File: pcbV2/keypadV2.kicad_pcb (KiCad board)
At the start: 2 copper layers, 93.7 x 93.3 mm, 78 parts, among them J1 Conn_01x02_Female, J2 USB_C_Receptacle, J3 Conn_01x03_Male, Q1 Q_NMOS_GSD, SW1 SW_Push, SW10 SW_Push, SW11 SW_Push, SW12 SW_Push, SW13 SW_SPDT, SW14 SW_Push, SW15 SW_Push, SW16 SW_Push, SW17 SW_DIP_x03, SW2 SW_Push, SW3 SW_Push, SW4 SW_Push, SW5 SW_Push, SW6 SW_Push, SW7 SW_Push, SW8 SW_Push, SW9 SW_Push, U1 Teensy4.0, U2 Waveshare_OLED_RGB

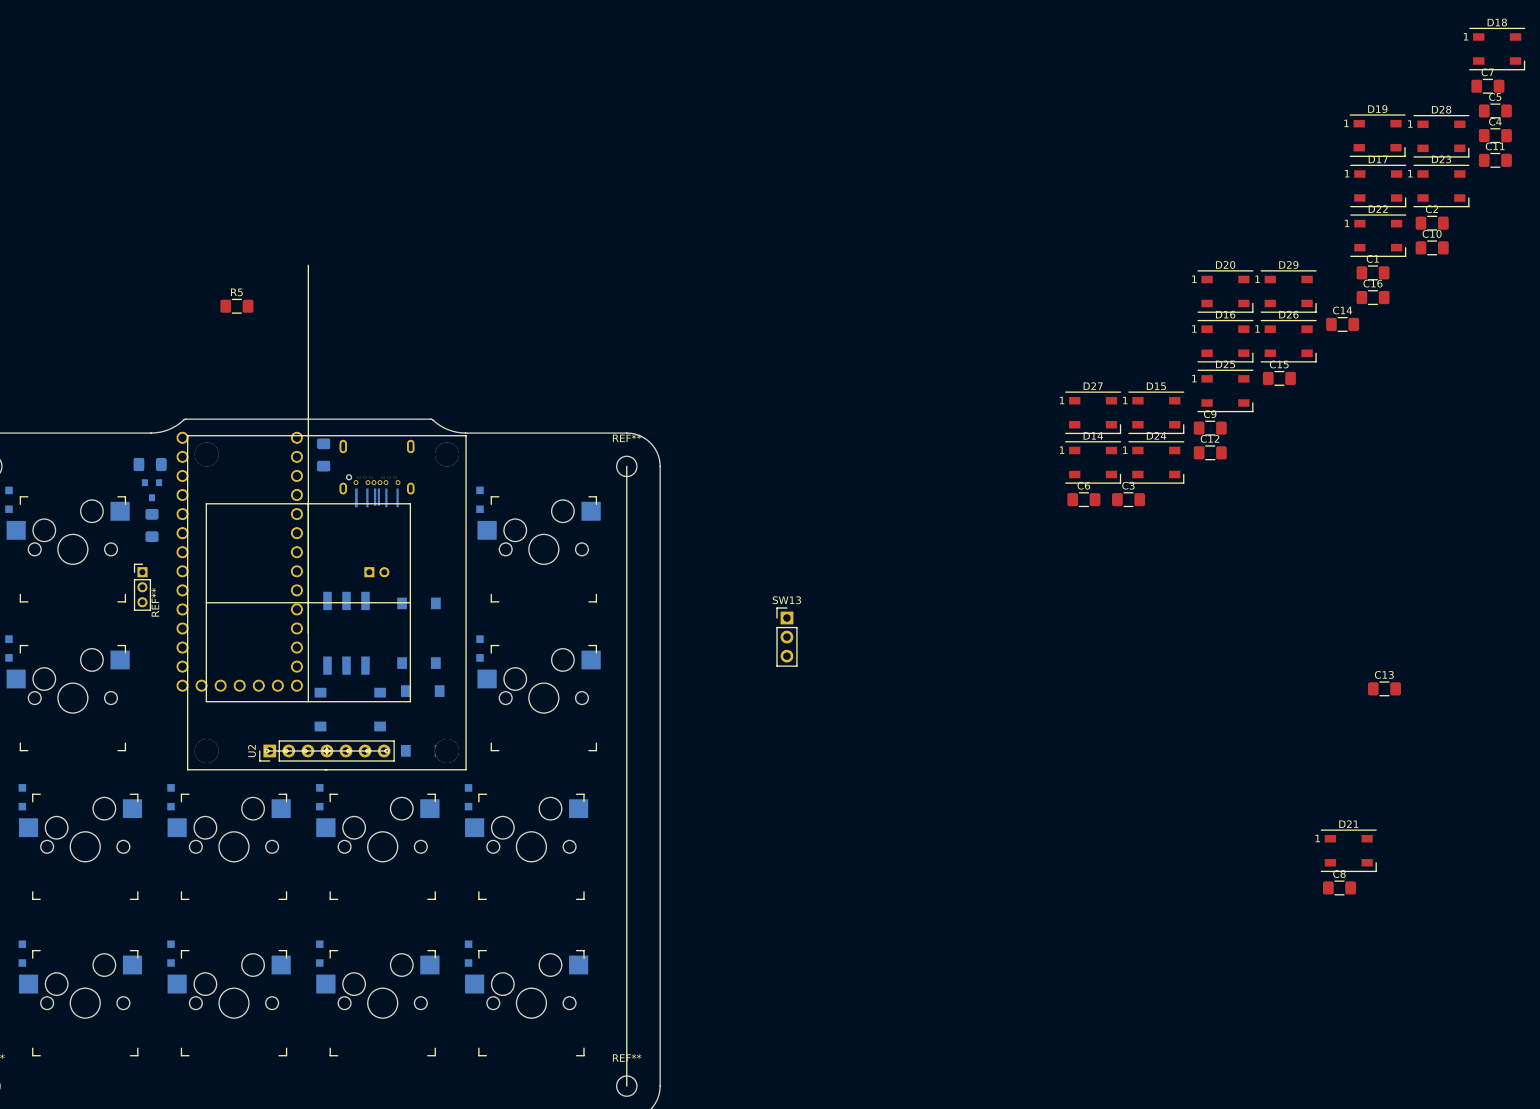
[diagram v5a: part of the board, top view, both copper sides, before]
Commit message: added ws2812b cutouts
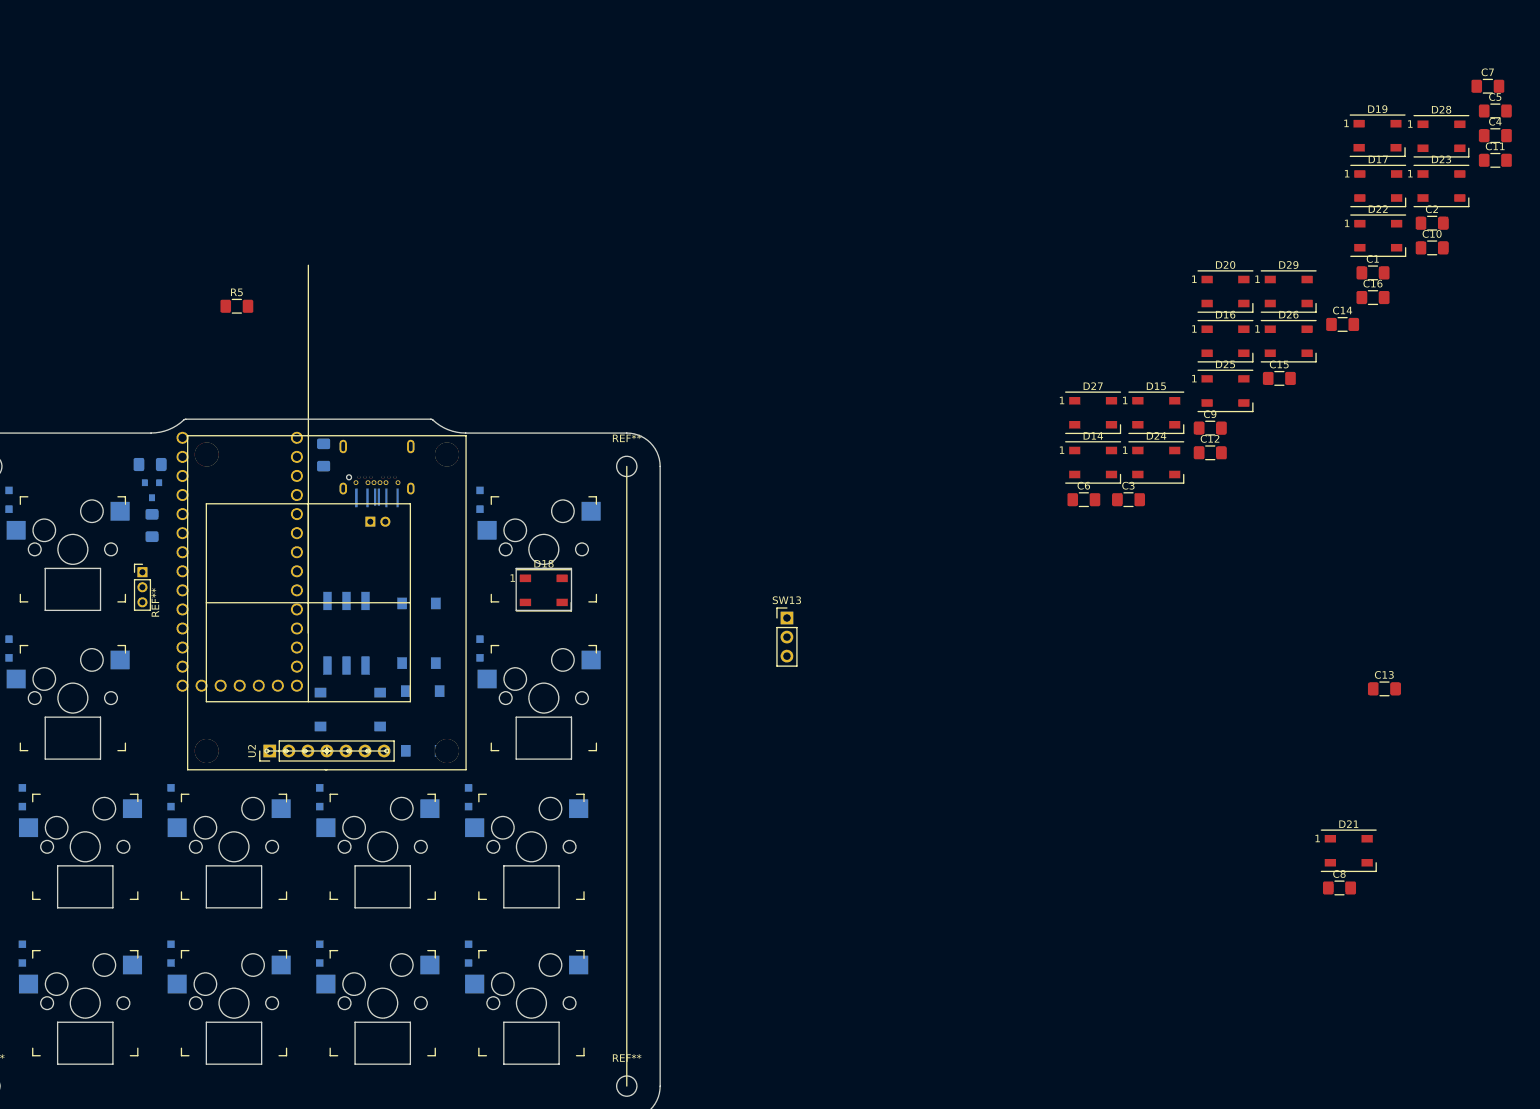
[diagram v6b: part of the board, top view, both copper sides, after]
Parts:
- moved D18 146.0 mm to (152.5, 123.3)
- moved J1 6.73 mm to (129.4, 114.2)
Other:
- outline, holes or cut-outs redrawn
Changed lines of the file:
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@@
   (general
     (thickness 1.6)
-    (drawings 25)
+    (drawings 73)
     (tracks 0)
     (zones 0)
@@
   )
   (module LED_SMD:LED_WS2812B_PLCC4_5.0x5.0mm_P3.2mm (layer F.Cu)
-    (at 279.516001 51.210001)
+    (at 152.527 123.317)
     (descr https://cdn-shop.adafruit.com/datasheets/WS2812B.pdf)
     (tags "LED RGB NeoPixel")
@@
   )
   (module Connector_PinHeader_2.00mm:PinHeader_1x02_P2.00mm_Vertical (layer B.Cu)
-    (at 129.286 120.904 270)
+    (at 129.413 114.173 270)
     (descr "Through hole straight pin header, 1x02, 2.00mm pitch, single row")
     (tags "Through hole pin header THT 1x02 2.00mm single row")
@@
       (net 52 ROW3))
   )
+  (gr_line (start 93.472 125.984) (end 93.472 120.396) (layer Edge.Cuts) (width 0.05))
+  (gr_line (start 86.106 125.984) (end 93.472 125.984) (layer Edge.Cuts) (width 0.05))
+  (gr_line (start 93.472 120.396) (end 86.106 120.396) (layer Edge.Cuts) (width 0.05))
+  (gr_line (start 86.106 120.396) (end 86.106 125.984) (layer Edge.Cuts) (width 0.05))
+  (gr_line (start 93.472 145.796) (end 93.472 140.208) (layer Edge.Cuts) (width 0.05))
+  (gr_line (start 86.106 145.796) (end 93.472 145.796) (layer Edge.Cuts) (width 0.05))
+  (gr_line (start 93.472 140.208) (end 86.106 140.208) (layer Edge.Cuts) (width 0.05))
+  (gr_line (start 86.106 140.208) (end 86.106 145.796) (layer Edge.Cuts) (width 0.05))
+  (gr_line (start 95.123 165.608) (end 95.123 160.02) (layer Edge.Cuts) (width 0.05))
+  (gr_line (start 87.757 165.608) (end 95.123 165.608) (layer Edge.Cuts) (width 0.05))
+  (gr_line (start 95.123 160.02) (end 87.757 160.02) (layer Edge.Cuts) (width 0.05))
+  (gr_line (start 87.757 160.02) (end 87.757 165.608) (layer Edge.Cuts) (width 0.05))
+  (gr_line (start 95.123 186.436) (end 95.123 180.848) (layer Edge.Cuts) (width 0.05))
+  (gr_line (start 87.757 186.436) (end 95.123 186.436) (layer Edge.Cuts) (width 0.05))
+  (gr_line (start 95.123 180.848) (end 87.757 180.848) (layer Edge.Cuts) (width 0.05))
+  (gr_line (start 87.757 180.848) (end 87.757 186.436) (layer Edge.Cuts) (width 0.05))
+  (gr_line (start 114.935 186.436) (end 114.935 180.848) (layer Edge.Cuts) (width 0.05))
+  (gr_line (start 107.569 186.436) (end 114.935 186.436) (layer Edge.Cuts) (width 0.05))
+  (gr_line (start 114.935 180.848) (end 107.569 180.848) (layer Edge.Cuts) (width 0.05))
+  (gr_line (start 107.569 180.848) (end 107.569 186.436) (layer Edge.Cuts) (width 0.05))
+  (gr_line (start 114.935 165.608) (end 114.935 160.02) (layer Edge.Cuts) (width 0.05))
+  (gr_line (start 107.569 165.608) (end 114.935 165.608) (layer Edge.Cuts) (width 0.05))
+  (gr_line (start 114.935 160.02) (end 107.569 160.02) (layer Edge.Cuts) (width 0.05))
+  (gr_line (start 107.569 160.02) (end 107.569 165.608) (layer Edge.Cuts) (width 0.05))
+  (gr_line (start 134.747 165.608) (end 134.747 160.02) (layer Edge.Cuts) (width 0.05))
+  (gr_line (start 127.381 165.608) (end 134.747 165.608) (layer Edge.Cuts) (width 0.05))
+  (gr_line (start 134.747 160.02) (end 127.381 160.02) (layer Edge.Cuts) (width 0.05))
+  (gr_line (start 127.381 160.02) (end 127.381 165.608) (layer Edge.Cuts) (width 0.05))
+  (gr_line (start 134.747 186.436) (end 134.747 180.848) (layer Edge.Cuts) (width 0.05))
+  (gr_line (start 127.381 186.436) (end 134.747 186.436) (layer Edge.Cuts) (width 0.05))
+  (gr_line (start 134.747 180.848) (end 127.381 180.848) (layer Edge.Cuts) (width 0.05))
+  (gr_line (start 127.381 180.848) (end 127.381 186.436) (layer Edge.Cuts) (width 0.05))
+  (gr_line (start 154.559 186.436) (end 154.559 180.848) (layer Edge.Cuts) (width 0.05))
+  (gr_line (start 147.193 186.436) (end 154.559 186.436) (layer Edge.Cuts) (width 0.05))
+  (gr_line (start 154.559 180.848) (end 147.193 180.848) (layer Edge.Cuts) (width 0.05))
+  (gr_line (start 147.193 180.848) (end 147.193 186.436) (layer Edge.Cuts) (width 0.05))
+  (gr_line (start 154.559 165.608) (end 154.559 160.02) (layer Edge.Cuts) (width 0.05))
+  (gr_line (start 147.193 165.608) (end 154.559 165.608) (layer Edge.Cuts) (width 0.05))
+  (gr_line (start 154.559 160.02) (end 147.193 160.02) (layer Edge.Cuts) (width 0.05))
+  (gr_line (start 147.193 160.02) (end 147.193 165.608) (layer Edge.Cuts) (width 0.05))
+  (gr_line (start 156.21 140.208) (end 148.844 140.208) (layer Edge.Cuts) (width 0.05))
+  (gr_line (start 148.844 145.796) (end 156.21 145.796) (layer Edge.Cuts) (width 0.05))
+  (gr_line (start 156.21 145.796) (end 156.21 140.208) (layer Edge.Cuts) (width 0.05))
+  (gr_line (start 148.844 140.208) (end 148.844 145.796) (layer Edge.Cuts) (width 0.05))
+  (gr_line (start 156.21 125.984) (end 156.21 120.396) (layer Edge.Cuts) (width 0.05))
+  (gr_line (start 148.844 125.984) (end 156.21 125.984) (layer Edge.Cuts) (width 0.05))
+  (gr_line (start 148.844 120.396) (end 148.844 125.984) (layer Edge.Cuts) (width 0.05))
+  (gr_line (start 156.21 120.396) (end 148.844 120.396) (layer Edge.Cuts) (width 0.05))
   (gr_line (start 163.576 102.362) (end 142.113 102.362) (layer Edge.Cuts) (width 0.05))
   (gr_line (start 137.483533 100.516942) (end 104.832467 100.516942) (layer Edge.Cuts) (width 0.05))

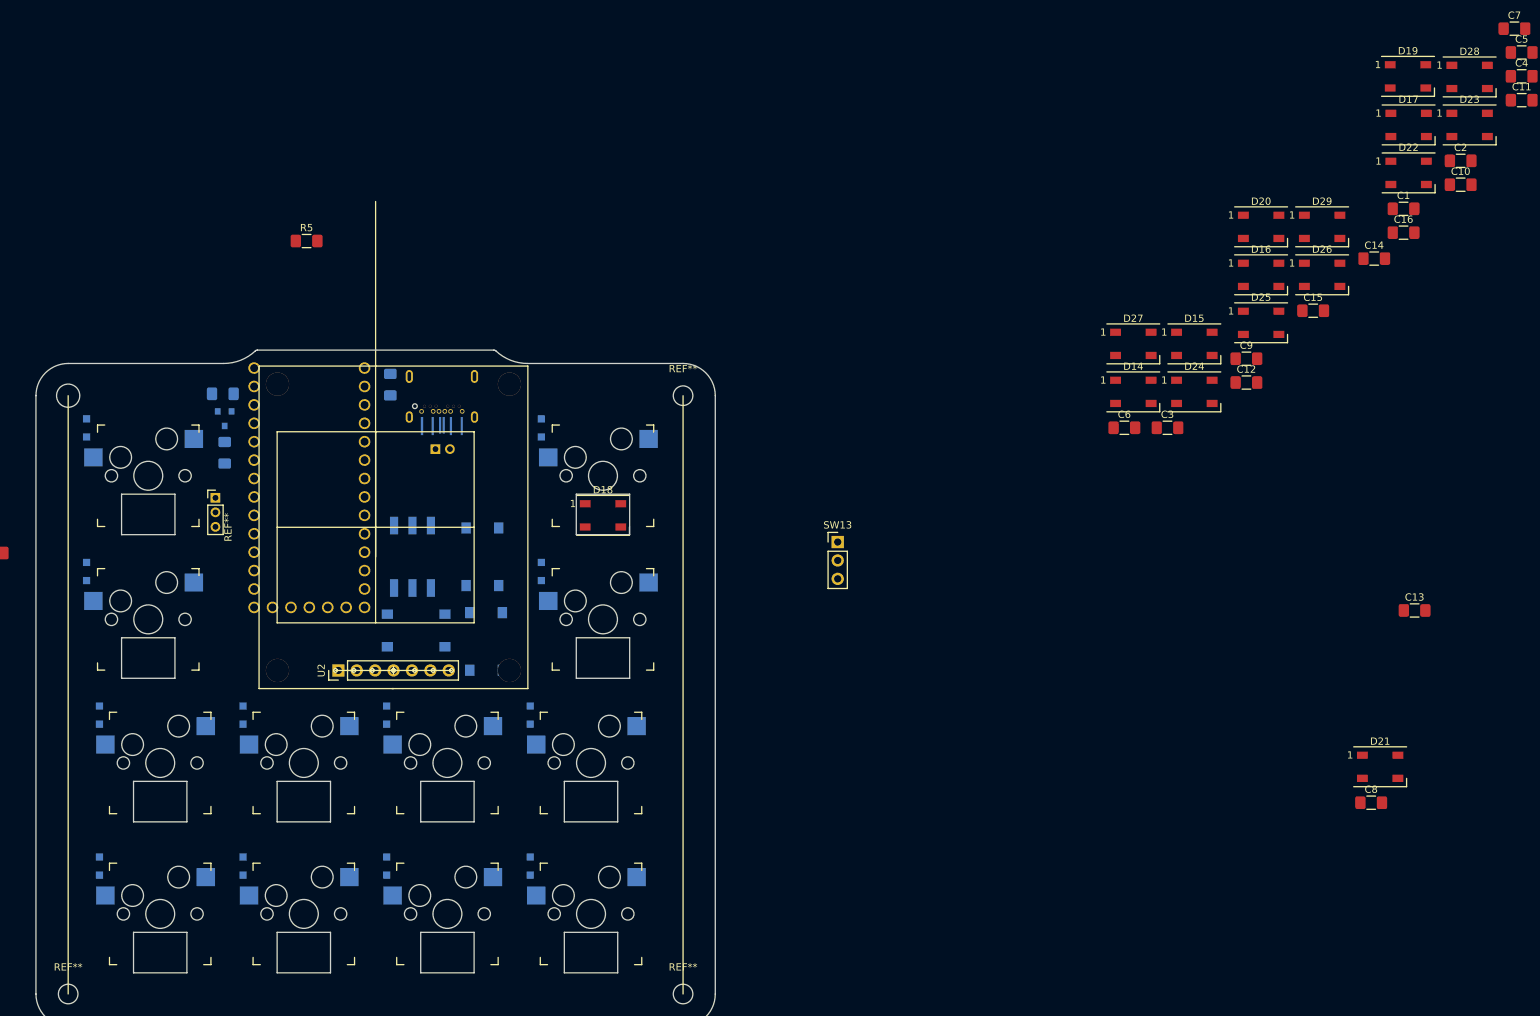
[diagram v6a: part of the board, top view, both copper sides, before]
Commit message: started layout of daughterboard
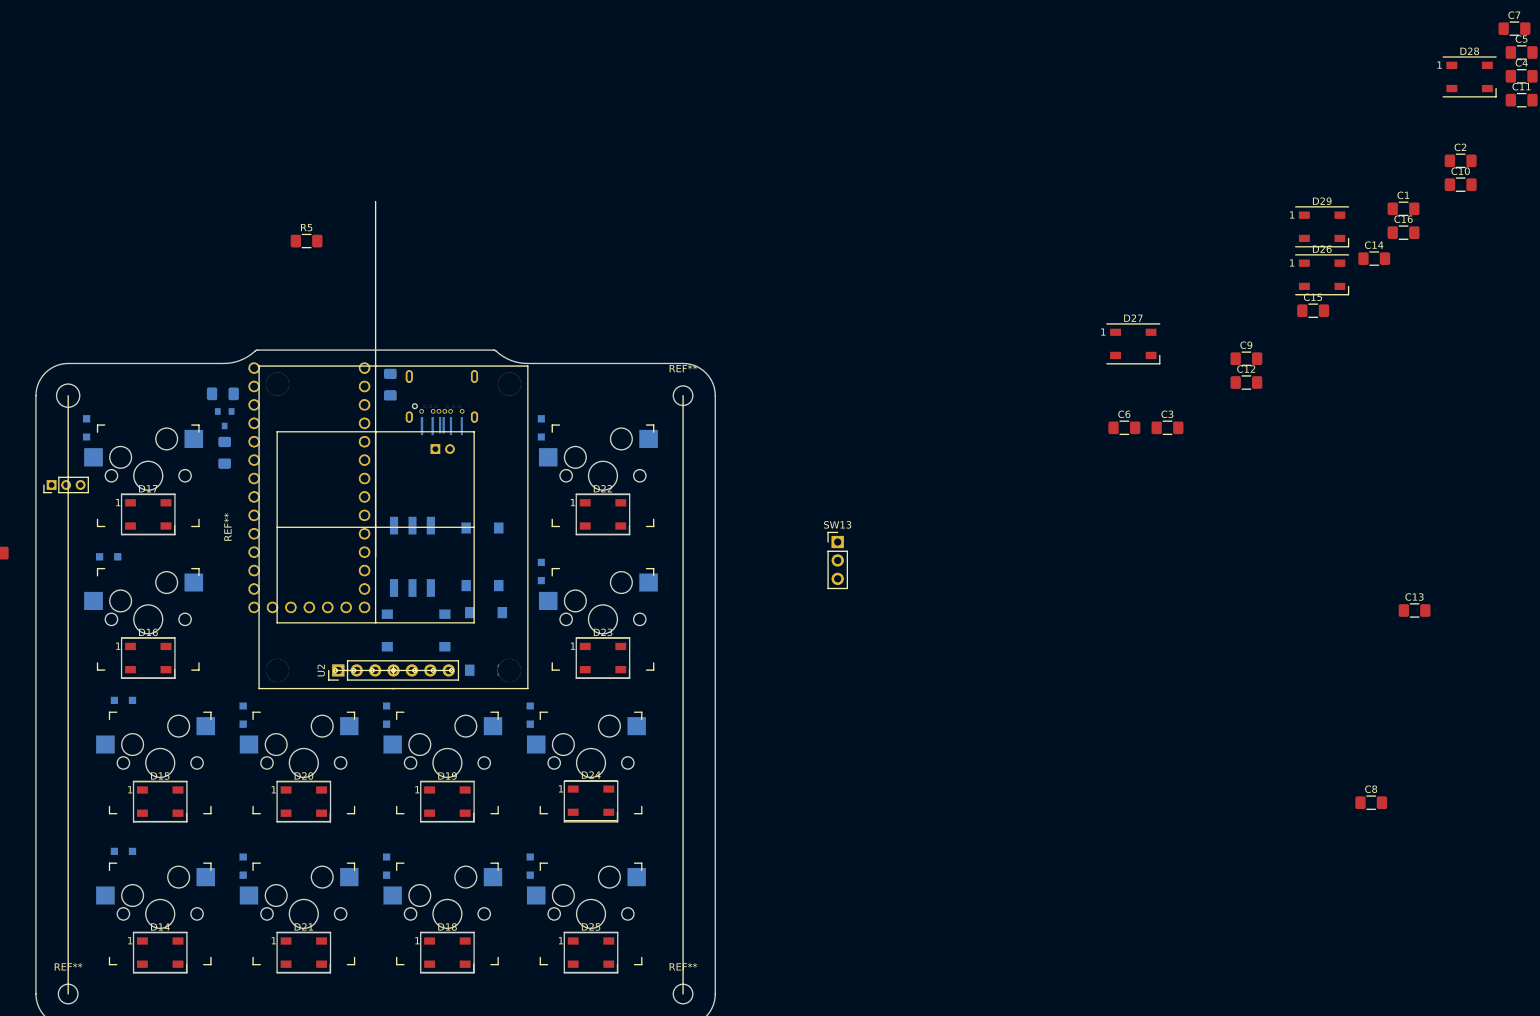
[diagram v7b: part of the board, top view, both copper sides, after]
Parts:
- SW1, SW10, SW11, SW12, SW2, SW3, SW4, SW5, SW6, SW7, SW8, SW9: footprint keyswitches:Kailh_socket_MX_RGB_cutout -> keyswitches:Kailh_socket_MX
- moved D17 182.0 mm to (89.8, 123.2)
- moved D19 166.1 mm to (131.1, 162.8)
- moved D16 162.4 mm to (89.8, 143.0)
- moved D15 156.0 mm to (91.4, 162.8)
- moved D14 155.0 mm to (91.4, 183.6)
- moved D20 154.1 mm to (111.3, 162.8)
- moved D21 150.7 mm to (111.3, 183.6)
- moved D23 140.4 mm to (152.5, 143.0)
- moved D25 126.9 mm to (150.9, 183.6)
- moved D22 120.7 mm to (152.5, 123.2)
- moved D24 100.6 mm to (150.9, 162.7)
- moved D18 64.0 mm to (131.1, 183.6)
- moved J3 22.7 mm to (76.5, 119.1), turned to 90 degrees
- moved D5 3.88 mm to (86.4, 148.8), turned to 180 degrees
- moved D9 3.88 mm to (86.4, 169.7), turned to 180 degrees
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
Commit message: .
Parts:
- added R6: JUMPER, Resistor_SMD:R_1206_3216Metric_Pad1.42x1.75mm_HandSolder, B.Cu at (95.5, 103.6)
- J3: footprint Connector_PinHeader_2.00mm:PinHeader_1x03_P2.00mm_Vertical -> Connector_PinHeader_2.54mm:PinHeader_1x03_P2.54mm_Vertical
- moved R3 12.0 mm to (91.4, 106.7), turned to 270 degrees
- moved Q1 5.08 mm to (96.3, 106.9), turned to 90 degrees
- moved R2 0.52 mm to (100.6, 106.7), turned to 270 degrees
